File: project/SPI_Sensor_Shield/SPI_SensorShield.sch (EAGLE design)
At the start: 23 parts, among them SW1 SKSGACE010

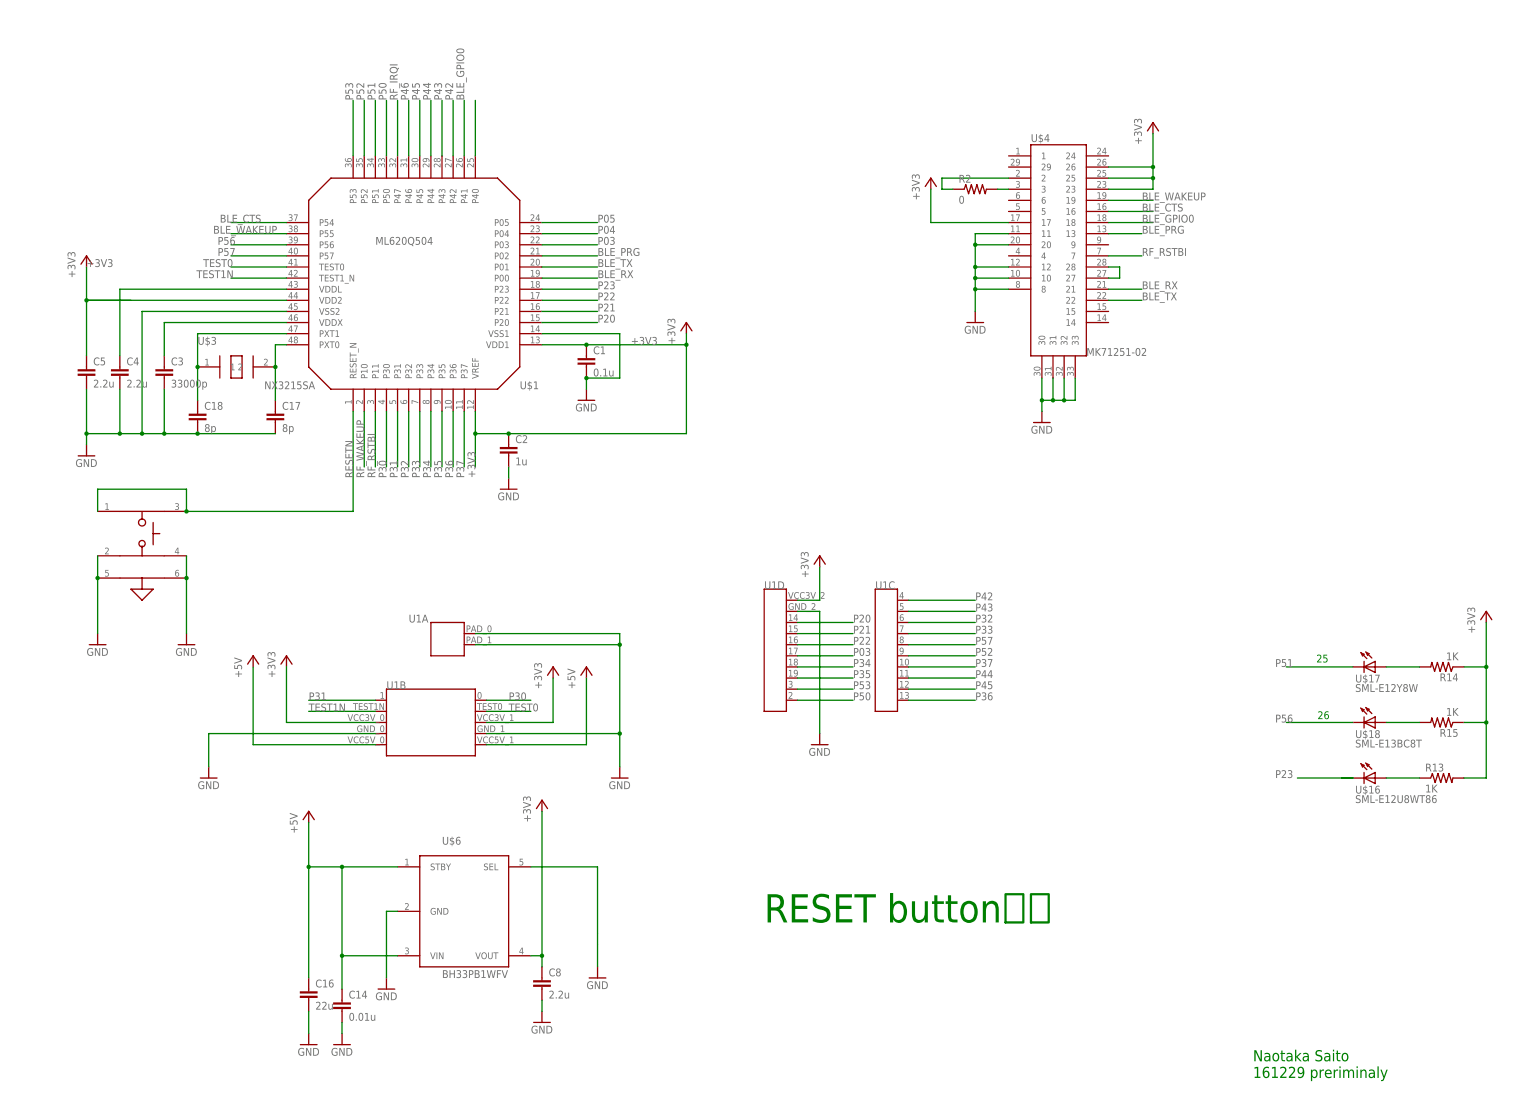
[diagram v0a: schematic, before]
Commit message: update libraries: add 1pin mark update Lazurite BLE: add silk of LOGO, board name, and pin number of Lazurite BLE. create SPI_Sensor_Shield.
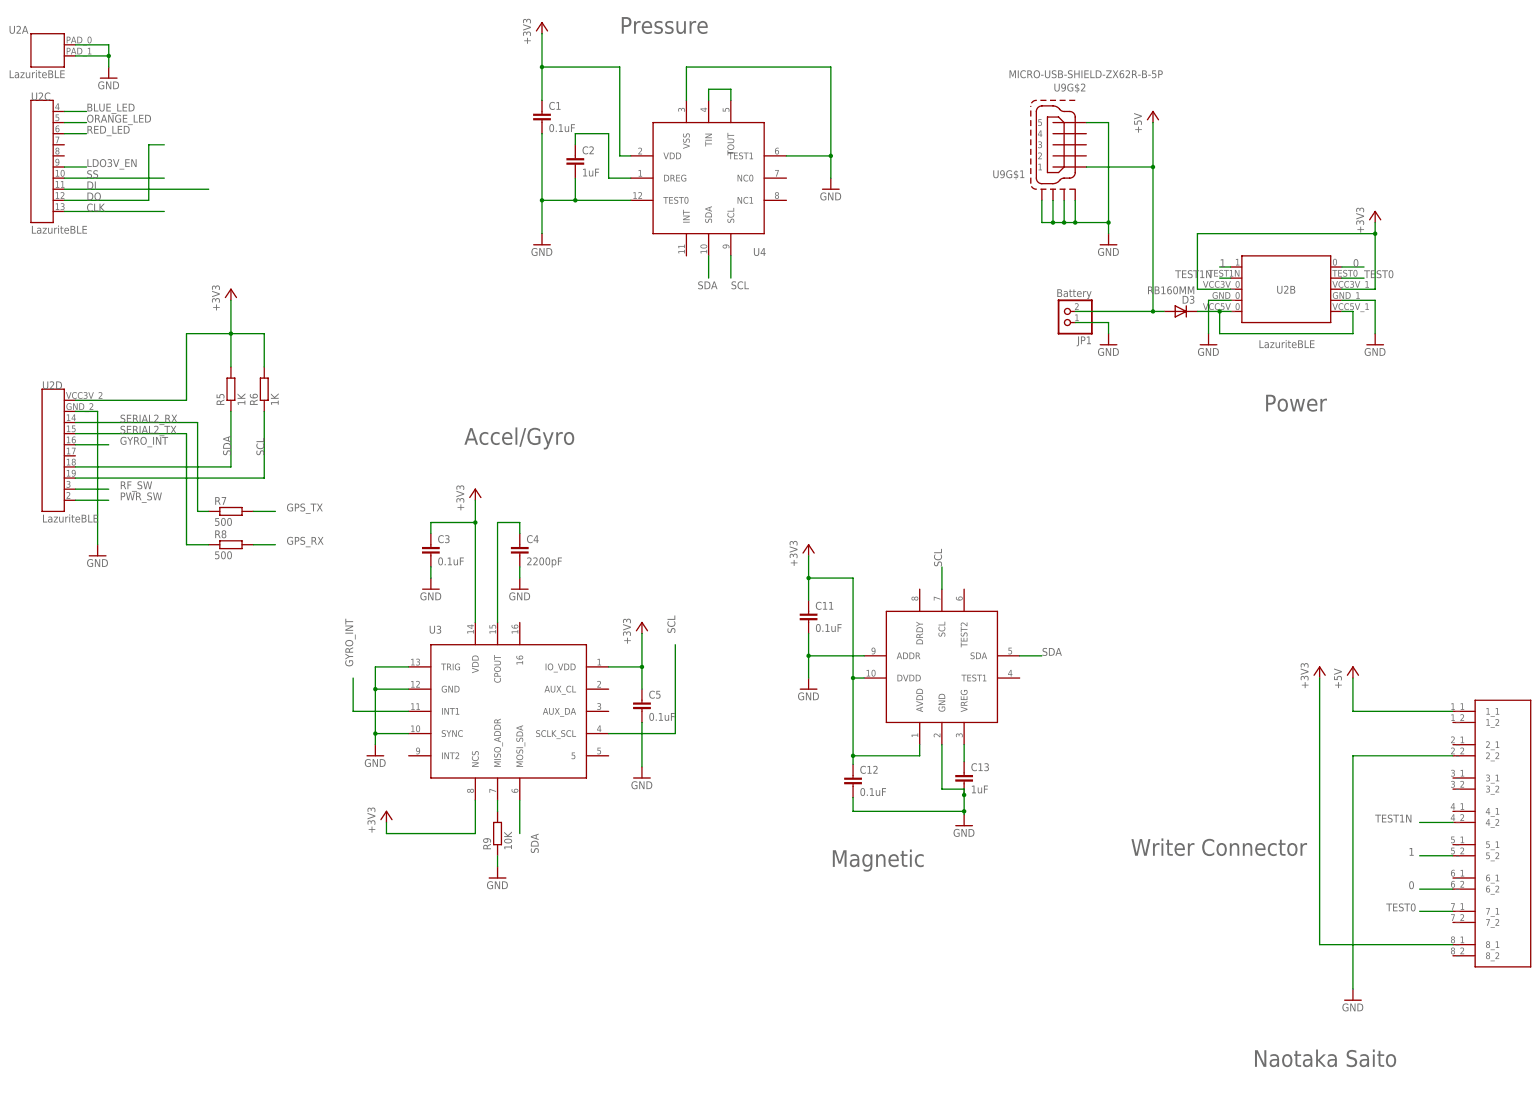
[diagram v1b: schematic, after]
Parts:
- removed C14: 0.01u, rcl:C-EUC0402
- removed C16: 22u, rcl:C-EUC1206
- removed C17, C18: 8p, rcl:C-EUC0402
- removed C8: 2.2u, rcl:C-EUC0402
- removed R13, R14, R15: 1K, rcl:R-US_R0402
- removed R2: 0, rcl:R-US_R0402
- removed SW1: SKSGACE010, lz-shield:SKSGACE010
- removed U$16: SML-E12U8WT86, lazurite:SML-E1X
- removed U$17: SML-E12Y8W, lazurite:SML-E1X
- removed U$18: SML-E13BC8T, lazurite:SML-E1X
- removed U$3: NX3215SA, lazurite:NX3215SA
- removed U$4: MK71251-02, lz-shield:MK71251-02
- removed U$6: BH33PB1WFV, lazurite:BHXXPB1WFV
- removed U1: (no value), lazurite:LAZURITE920J
- added C11, C12: 0.1uF, rcl:C-EUC0603
- added C13: 1uF, rcl:C-EUC0603
- added D3: RB160MM, lazurite:RB160MM
- added JP1: Battery, pinhead:PINHD-1X2
- added R5, R6: 1K, rcl:R-EU_R0603
- added R7, R8: 500, rcl:R-EU_R0603
- added R9: 10K, rcl:R-EU_R0603
- added U2: LazuriteBLE, lazurite:LAZURITE920JLAZURITE920J
- added U3: KXG03, lz-shield:KXG03
- added U4: BM1383AGLV, lz-shield:BM1383AGLV
- added U8: BM1422AGMV, lz-shield:BM1422AGMV
- added U9: MICRO-USB-SHIELD-ZX62R-B-5P, con-hirose:MICRO-USB-SHIELD-ZX62R-B-5P
- C1: value 0.1u -> 0.1uF; device rcl:C-EUC0402 -> rcl:C-EUC0603
- C2: value 1u -> 1uF; device rcl:C-EUC0402 -> rcl:C-EUC0603
- C3: value 33000p -> 0.1uF; device rcl:C-EUC0402 -> rcl:C-EUC0603
- C4: value 2.2u -> 2200pF; device rcl:C-EUC0402 -> rcl:C-EUC0603
- C5: value 2.2u -> 0.1uF; device rcl:C-EUC0402 -> rcl:C-EUC0603
- U$1: value ML620Q504 -> XB-1-X; device lazurite:ML620Q504 -> lz-shield:XB-1-X
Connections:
- removed net BLE_CTS: U$1.P54, U$4.16
- removed net BLE_GPIO0: U$1.P41, U$4.18
- removed net BLE_PRG: U$1.P02, U$4.13
- removed net BLE_RX: U$1.P00, U$4.21
- removed net BLE_TX: U$1.P01, U$4.22
- removed net BLE_WAKEUP: U$1.P55, U$4.19
- removed net N$1: C17.1, U$1.PXT0, U$3.2
- removed net N$19: R13.1, U$16.A
- removed net N$2: C18.1, U$1.PXT1, U$3.1
- removed net N$22: R15.2, U$18.A
- removed net N$32: R2.1, U$4.2
- removed net N$33: U$4.27, U$4.28
- removed net N$4: R2.2, U$4.3
- removed net P03: U$1.P03, U1D.17
- removed net P04: U$1.P04
- removed net P05: U$1.P05
- removed net P20: U$1.P20, U1D.14
- removed net P21: U$1.P21, U1D.15
- removed net P22: U$1.P22, U1D.16
- removed net P23: U$1.P23, U$16.C
- removed net P30: U$1.P30, U1B.0
- removed net P31: U$1.P31, U1B.1
- removed net P32: U$1.P32, U1C.6
- removed net P33: U$1.P33, U1C.7
- removed net P34: U$1.P34, U1D.18
- removed net P35: U$1.P35, U1D.19
- removed net P36: U$1.P36, U1C.13
- removed net P37: U$1.P37, U1C.10
- removed net P42: U$1.P42, U1C.4
- removed net P43: U$1.P43, U1C.5
- removed net P44: U$1.P44, U1C.11
- removed net P45: U$1.P45, U1C.12
- removed net P46: U$1.P46
- removed net P50: U$1.P50, U1D.2
- removed net P51: U$1.P51, U$17.C
- removed net P52: U$1.P52, U1C.9
- removed net P53: U$1.P53, U1D.3
- removed net P56: U$1.P56, U$18.C
- removed net P57: U$1.P57, U1C.8
- removed net RESETN: SW1.1, SW1.3, U$1.RESET_N
- removed net RF_IRQI: U$1.P47
- removed net RF_RSTBI: U$1.P11, U$4.7
- removed net RF_WAKEUP: U$1.P10
- removed net SDA0I: U$1.P40
- new net 0: U$1.6_2, U2B.0
- new net 1: U$1.5_2, U2B.1
- new net BLUE_LED: U2C.4
- new net CLK: U2C.13
- new net DI: U2C.11
- new net DO: U2C.12
- new net GPS_RX: R8.2
- new net GPS_TX: R7.2
- new net GYRO_INT: U2D.16, U3.INT1
- new net LDO3V_EN: U2C.9
- new net N$10: D3.C, U2B.VCC5V_0, U2B.VCC5V_1
- new net N$15: C13.1, U8.VREG
- new net N$16: C4.1, U3.CPOUT
- new net ORANGE_LED: U2C.5
- new net PWR_SW: U2D.2
- new net RED_LED: U2C.6
- new net RF_SW: U2D.3
- new net SCL: R6.1, U2D.19, U3.SCLK_SCL, U4.SCL, U8.SCL
- new net SDA: R5.1, U2D.18, U3.MOSI_SDA, U4.SDA, U8.SDA
- new net SERIAL2_RX: R7.1, U2D.14
- new net SERIAL2_TX: R8.1, U2D.15
- new net SS: U2C.10
- net +3V3: now also C11.1, C12.1, C3.1, R5.2, R6.2, U$1.8_1, U2B.VCC3V_0, U2B.VCC3V_1, U2D.VCC3V_2, U3.IO_VDD, U3.NCS, U3.VDD, U4.VDD, U8.AVDD, U8.DVDD; no longer C2.1, C8.1, R13.2, R14.1, R15.1, U$1.VDD1, U$1.VDD2, U$1.VREF, U$4.17, U$4.23, U$4.25, U$4.26, U$6.VOUT, U1B.VCC3V_0, U1B.VCC3V_1, U1D.VCC3V_2
- net +5V: now also D3.A, JP1.2, U$1.1_1, U9G$2.1; no longer C14.1, C16.1, U$6.STBY, U$6.VIN, U1B.VCC5V_0, U1B.VCC5V_1
- net GND: now also C11.2, C12.2, C13.2, JP1.1, R9.1, U$1.2_2, U2A.PAD_0, U2A.PAD_1, U2B.GND_0, U2B.GND_1, U2D.GND_2, U3.GND, U3.SYNC, U3.TRIG, U4.TEST0, U4.TEST1, U4.VSS, U8.ADDR, U8.GND, U9G$1.S1, U9G$1.S2, U9G$1.S3, U9G$1.S4, U9G$2.5; no longer C14.2, C16.2, C17.2, C18.2, C8.2, SW1.2, SW1.4, SW1.5, SW1.6, U$1.VSS1, U$1.VSS2, U$4.10, U$4.11, U$4.12, U$4.20, U$4.30, U$4.31, U$4.32, U$4.33, U$4.8, U$6.GND, U$6.SEL, U1A.PAD_0, U1A.PAD_1, U1B.GND_0, U1B.GND_1, U1D.GND_2
- net N$3: now also U4.TIN, U4.TOUT; no longer C3.1, U$1.VDDX
- net N$5: now also R9.2, U3.MISO_ADDR; no longer R14.2, U$17.A
- net N$7: now also C2.1, U4.DREG; no longer C4.1, U$1.VDDL
- net TEST0: now also U$1.7_1, U2B.TEST0; no longer U$1.TEST0, U1B.TEST0
- net TEST1N: now also U$1.4_2, U2B.TEST1N; no longer U$1.TEST1_N, U1B.TEST1N
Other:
- note added: "Accel/Gyro"
- note added: "Magnetic"
- note added: "Naotaka Saito"
- note added: "Power"
- note added: "Pressure"
- note added: "Writer Connector"
- note removed: "25"
- note removed: "26"
- note removed: "Naotaka Saito 161229 preriminaly"
- note removed: "RESET button追加"
- moved on the sheet: C1, C2, C3, C4, C5
